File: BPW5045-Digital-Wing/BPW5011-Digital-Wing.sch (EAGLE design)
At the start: 3 parts

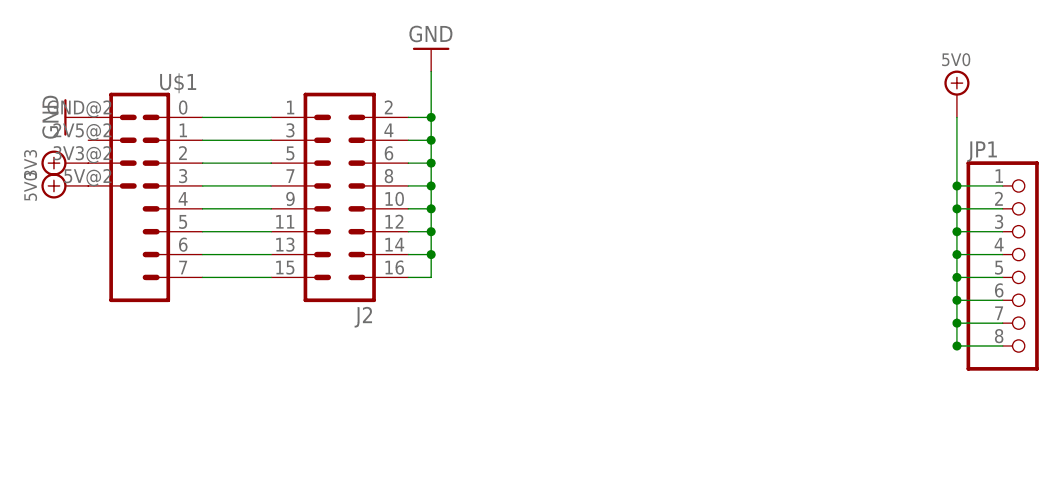
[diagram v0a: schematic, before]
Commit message: Update Digital Wing to use Grove Connectors
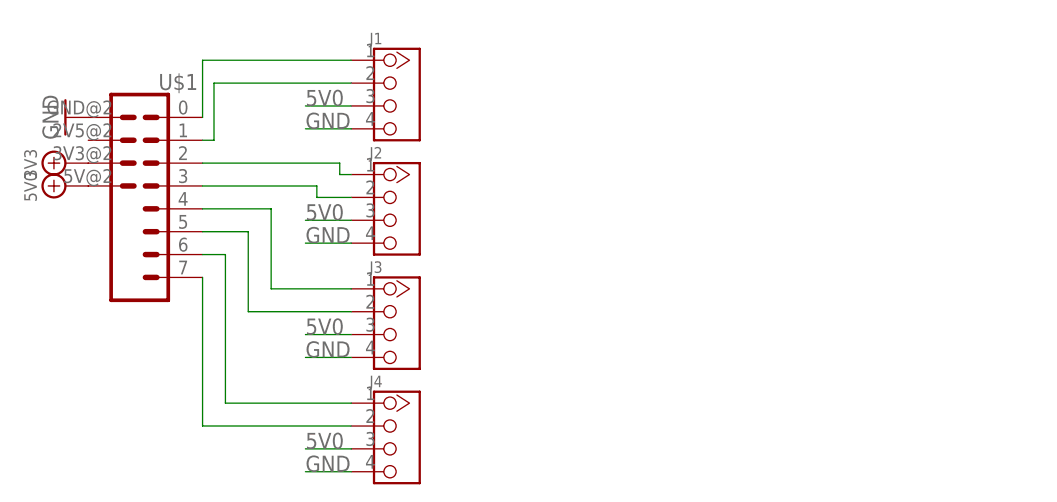
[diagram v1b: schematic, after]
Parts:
- removed JP1: (no value), GadgetFactory:PINHD-1X8
- added J1, J3, J4: (no value), GadgetFactory_6.0:CONNECTOR_TWIG-2.0-LEADED
- J2: device con-lstb:MA08-2 -> GadgetFactory_6.0:CONNECTOR_TWIG-2.0-LEADED
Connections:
- net 5V0: now also J1.3, J2.3, J3.3, J4.3; no longer JP1.1, JP1.2, JP1.3, JP1.4, JP1.5, JP1.6, JP1.7, JP1.8
- net GND: now also J1.4, J3.4, J4.4; no longer J2.10, J2.12, J2.14, J2.16, J2.2, J2.6, J2.8
- net N$1: now also J1.1; no longer J2.1
- net N$2: now also J1.2; no longer J2.3
- net N$3: now also J2.1; no longer J2.5
- net N$4: now also J2.2; no longer J2.7
- net N$5: now also J3.1; no longer J2.9
- net N$6: now also J3.2; no longer J2.11
- net N$7: now also J4.1; no longer J2.13
- net N$8: now also J4.2; no longer J2.15

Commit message: Add 5V resistors for Digital Grove Wing
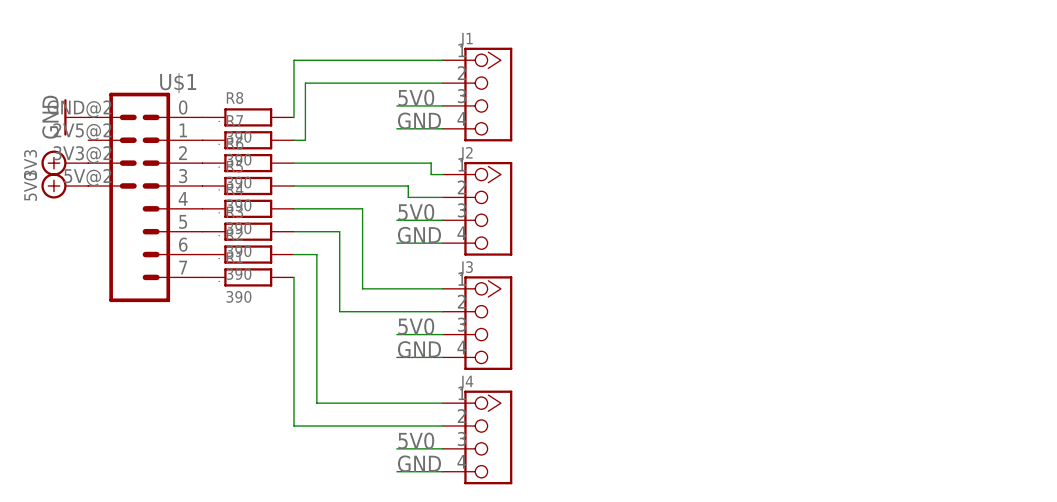
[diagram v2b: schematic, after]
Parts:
- added R1, R2, R3, R4, R5, R6, R7, R8: 390, GadgetFactory:R0805
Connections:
- new net N$10: R2A.1, U$1.7
- new net N$11: R3A.1, U$1.6
- new net N$12: R4A.1, U$1.5
- new net N$13: R5A.1, U$1.4
- new net N$14: R6A.1, U$1.3
- new net N$15: R7A.1, U$1.2
- new net N$16: R8A.1, U$1.1
- new net N$9: R1A.1, U$1.8
- net N$1: now also R8A.2; no longer U$1.1
- net N$2: now also R7A.2; no longer U$1.2
- net N$3: now also R6A.2; no longer U$1.3
- net N$4: now also R5A.2; no longer U$1.4
- net N$5: now also R4A.2; no longer U$1.5
- net N$6: now also R3A.2; no longer U$1.6
- net N$7: now also R2A.2; no longer U$1.7
- net N$8: now also R1A.2; no longer U$1.8
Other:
- moved on the sheet: J1, J2, J3, J4
